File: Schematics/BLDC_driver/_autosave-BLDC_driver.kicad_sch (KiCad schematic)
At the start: 70 parts, among them J1 DA15_Plug_MountingHoles, J2 Display connectors, J3 Programmer IO, J4 unused pins, J5 DE9_Receptacle_MountingHoles, J6 Conn_01x07_Pin, J7 USB_B_Micro, Q1 2N7002, Q2 2N7002, Q3 2N7002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

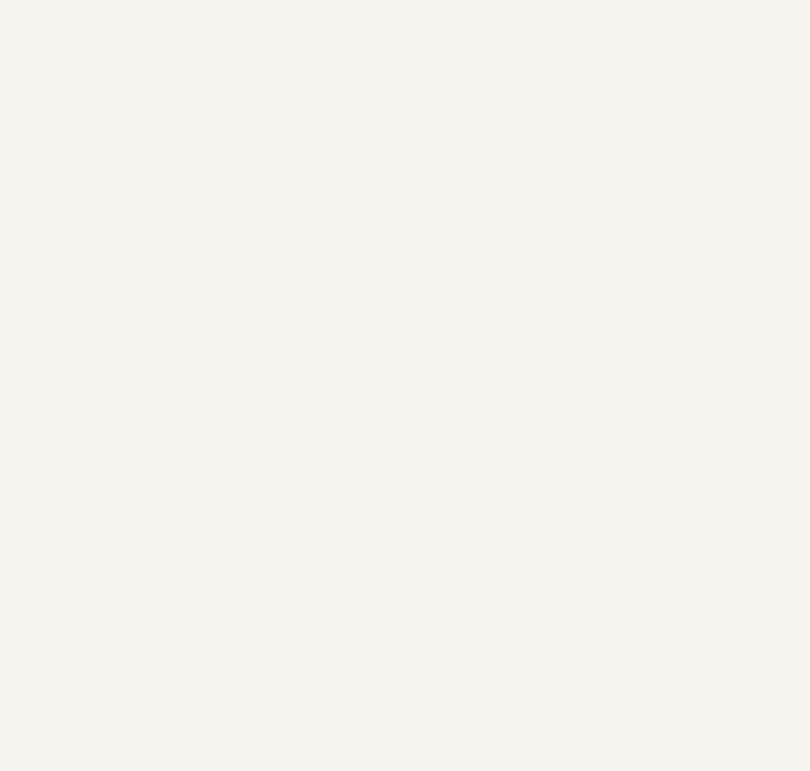
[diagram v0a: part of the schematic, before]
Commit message: Fixed incorrect diode
Switching regulator diode changed to zener from shottky (same footprint)
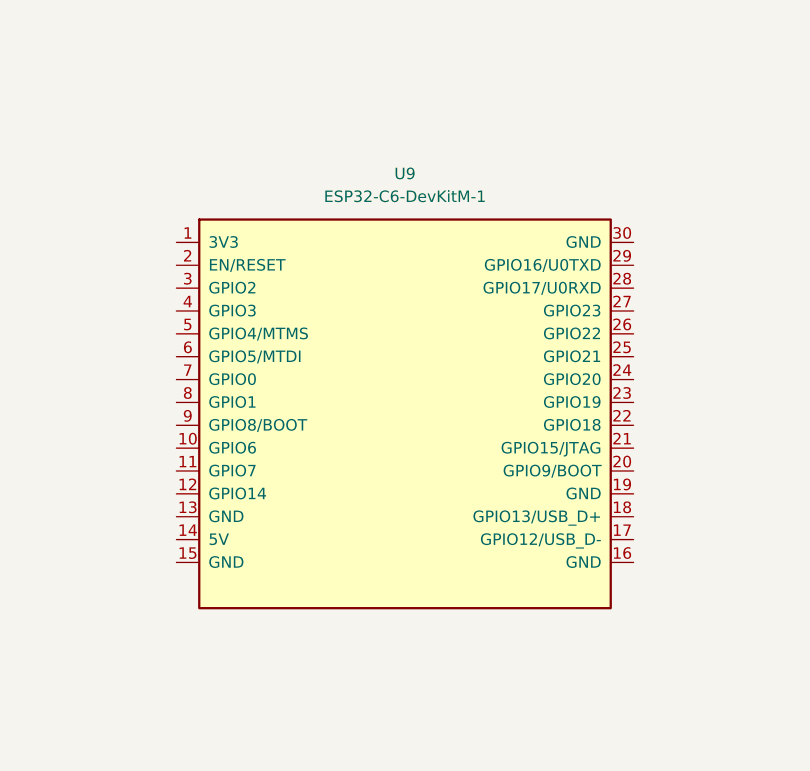
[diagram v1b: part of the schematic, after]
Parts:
- added U9: ESP32-C6-DevKitM-1, PCM_Espressif:ESP32-C6-DevKitM-1, symbol PCM_Espressif:ESP32-C6-DevKitM-1
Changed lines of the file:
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@@
+	)
+	(symbol
+		(lib_id "PCM_Espressif:ESP32-C6-DevKitM-1")
+		(at 336.55 153.67 0)
+		(unit 1)
+		(exclude_from_sim no)
+		(in_bom yes)
+		(on_board yes)
+		(dnp no)
+		(fields_autoplaced yes)
+		(property "Reference" "U9"
+			(at 336.55 128.27 0)
+			(effects
+				(font
+					(size 1.27 1.27)
+				)
+			)
+		)
+		(property "Value" "ESP32-C6-DevKitM-1"
+			(at 336.55 130.81 0)
+			(effects
+				(font
+					(size 1.27 1.27)
+				)
+			)
+		)
+		(property "Footprint" "PCM_Espressif:ESP32-C6-DevKitM-1"
+			(at 336.55 179.07 0)
+			(effects
+				(font
+					(size 1.27 1.27)
+				)
+				(hide yes)
+			)
+		)
+		(property "Datasheet" "https://docs.espressif.com/projects/espressif-esp-dev-kits/en/latest/esp32c6/esp32-c6-devkitm-1/index.html"
+			(at 345.44 181.61 0)
+			(effects
+				(font
+					(size 1.27 1.27)
+				)
+				(hide yes)
+			)
+		)
+		(property "Description" "ESP32-C6-DevKitC-1"
+			(at 336.55 153.67 0)
+			(effects
+				(font
+					(size 1.27 1.27)
+				)
+				(hide yes)
+			)
+		)
+		(pin "15"
+		)
+		(pin "27"
+		)
+		(pin "5"
+		)
+		(pin "21"
+		)
+		(pin "7"
+		)
+		(pin "28"
+		)
+		(pin "6"
+		)
+		(pin "30"
+		)
+		(pin "26"
+		)
+		(pin "14"
+		)
+		(pin "16"
+		)
+		(pin "19"
+		)
+		(pin "4"
+		)
+		(pin "22"
+		)
+		(pin "8"
+		)
+		(pin "23"
+		)
+		(pin "1"
+		)
+		(pin "9"
+		)
+		(pin "2"
+		)
+		(pin "12"
+		)
+		(pin "10"
+		)
+		(pin "11"
+		)
+		(pin "13"
+		)
+		(pin "24"
+		)
+		(pin "17"
+		)
+		(pin "29"
+		)
+		(pin "18"
+		)
+		(pin "25"
+		)
+		(pin "20"
+		)
+		(pin "3"
+		)
+		(instances
+			(project ""
+				(path "/26e46729-b0c8-4f6b-9483-46042ba84cb9"
+					(reference "U9")
+					(unit 1)
+				)
+			)
+		)
 	)
 	(symbol
